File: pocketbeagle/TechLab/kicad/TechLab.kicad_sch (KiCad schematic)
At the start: 82 parts, among them T1 3904, T2 EAALSTIC1708A0, U1 CAT24C32, U2 TPD4S012DRY, U3 MMA8453Q, U4 TPS2051CDBV, U5 MCP23S18-E/MJ, U6 FT230XQ-R, X1 292303-1, X2 10118192-0001LF

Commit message: Convert Techlab to multisheet schematic
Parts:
- removed BUZZER0: SMD-140035H, TechLab:SMD-140035H, symbol TechLab-eagle-import:SMD-140035H
- removed C1, C10, C2, C3, C4, C5, C8, C9: .1uF, TechLab:0402, symbol TechLab-eagle-import:CAPACITOR-(INCH)-0402
- removed C11: 10nF, TechLab:0402, symbol TechLab-eagle-import:CAPACITOR-(INCH)-0402
- removed C6: 4.7uF, TechLab:0402, symbol TechLab-eagle-import:CAPACITOR-(INCH)-0402
- removed C7: 10uF, 6.3V, TechLab:0805, symbol TechLab-eagle-import:CAPACITOR-(INCH)-0805
- removed EXP1: PARALLEL-8PIN-0.9INCH_PITCH-SMT_GP, TechLab:PARALLEL-8PIN-0.9INCH_PITCH-SMT_GP, symbol TechLab-eagle-import:PARALLEL-8PIN-0.9INCH_PITCH-SMT_GP
- removed F1, F2: 1206L025YR, TechLab:1206, symbol TechLab-eagle-import:FUSE-(INCH)-1206
- removed FB1, FB2, FB3, FB4: 120 Ohm (BLM18AG121SN1D), TechLab:0603, symbol TechLab-eagle-import:FB-(INCH)-0603
- removed FUD1, FUD2, FUD3: FIDUCIAL, TechLab:FIDUCIAL_40MIL, symbol TechLab-eagle-import:FIDUCIAL
- removed JMP1: JUMPER-(X2), TechLab:JUMPER-(X2), symbol TechLab-eagle-import:JUMPER-(X2)
- removed L.BTN0, R.BTN0: TACTILE.SWITCH-6MM, TechLab:6MM_TACTILE-SWITCH, symbol TechLab-eagle-import:TACTILE.SWITCH-6MM
- removed LD1: JNS-5050RGB, TechLab:LED_RGB_5050, symbol TechLab-eagle-import:JNS-5050RGB
- removed LD10, LD11, LD12, LD13, LD14, LD15, LD2, LD3, LD4, LD5, LD6, LD7, LD8, LD9, TX0: GREEN, TechLab:0805-LED, symbol TechLab-eagle-import:LED-(INCH)-0805
- removed POCKETBEAGLE-1: POCKETBEAGLE-(ORIGIN-CENTER)-SMT.PADS(ONLY)-NO.RE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, TechLab:POCKETBEAGLE-(ORIGIN-CENTER)-SMT.PADS(ONLY)-NO.RESTRICT, symbol TechLab-eagle-import:POCKETBEAGLE-(ORIGIN-CENTER)-SMT.PADS(ONLY)-NO.RESTRICT
- removed R1, R2: 1.5k, TechLab:0402, symbol TechLab-eagle-import:RESISTOR-(INCH)-0402
- removed R10, R19, R20, R9: 33, TechLab:0402, symbol TechLab-eagle-import:RESISTOR-(INCH)-0402
- removed R11, R12, R13, R14, R21, R22, R3, R4: 1k, TechLab:0402, symbol TechLab-eagle-import:RESISTOR-(INCH)-0402
- removed R15, R16: DNP(2.2k), TechLab:0402, symbol TechLab-eagle-import:RESISTOR-(INCH)-0402
- removed R17, R18, R5: 4.7k, TechLab:0402, symbol TechLab-eagle-import:RESISTOR-(INCH)-0402
- removed R6: 100k, TechLab:0402, symbol TechLab-eagle-import:RESISTOR-(INCH)-0402
- removed R7: DNP(1.5k), TechLab:0402, symbol TechLab-eagle-import:RESISTOR-(INCH)-0402
- removed R8: 0, TechLab:0402, symbol TechLab-eagle-import:RESISTOR-(INCH)-0402
- removed RESET.BTN0: TACTILE.SWITCH-3X3.5MM, TechLab:3X3.5MM-TACTILE-SWITCH, symbol TechLab-eagle-import:TACTILE.SWITCH-3X3.5MM
- removed RN1, RN2, RN3, RN4: 1k, TechLab:RN0804, symbol TechLab-eagle-import:RESISTOR.NETWORK-(4)
- removed RX0: RED, TechLab:0805-LED, symbol TechLab-eagle-import:LED-(INCH)-0805
- removed SJ1, SJ2: SOLDER.JOINT-(INCH)-0402, TechLab:SOLDER.JOINT(0402), symbol TechLab-eagle-import:SOLDER.JOINT-(INCH)-0402
- removed T1: 3904, TechLab:SOT23, symbol TechLab-eagle-import:NPN.BIPOLAR-(SOT23)
- removed T2: EAALSTIC1708A0, TechLab:EAALSTIC1708A0, symbol TechLab-eagle-import:EAALSTIC1708A0
- removed U1: CAT24C32, TechLab:UDFN8,2X3(ON-SEMI), symbol TechLab-eagle-import:CAT24C32
- removed U2: TPD4S012DRY, TechLab:SON-6(TI)-DRY, symbol TechLab-eagle-import:TPD4S012DRYR
- removed U3: MMA8453Q, TechLab:QFN-16-(MMA8453Q), symbol TechLab-eagle-import:MMA8453Q
- removed U4: TPS2051CDBV, TechLab:SOT23-5(TI-DBV), symbol TechLab-eagle-import:TPS2051CDBV
- removed U5: MCP23S18-E/MJ, TechLab:QFN24-MJ-0.5-4X4MM, symbol TechLab-eagle-import:MCP23S18
- removed U6: FT230XQ-R, TechLab:QFN16-0.65-4X4MM, symbol TechLab-eagle-import:FT230XQ
- removed X1: 292303-1, TechLab:292303-1, symbol TechLab-eagle-import:292303-1
- removed X2: 10118192-0001LF, TechLab:10118192-0001LF(MICRO-USB-B-AMPHENOL-FCI), symbol TechLab-eagle-import:10118192-0001LF
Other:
- added sheet Page1 (TechLab_page1.kicad_sch)
- added sheet Page2 (TechLab_Page2.kicad_sch)
- note removed: "------------------------------"
- note removed: "0 | 1 | 0 | 1 | A2 | A1 | A0 | R/W"
- note removed: "1 | 0 | 1 | 0 | H | H | H | R/W = 0x57"
- note removed: "1 | 0 | 1 | 0 | H | H | L | R/W = 0x56"
- note removed: "1 | 0 | 1 | 0 | H | L | H | R/W = 0x55"
- note removed: "1 | 0 | 1 | 0 | H | L | L | R/W = 0x54"
- note removed: "1 | 0 | 1 | 0 | L | H | H | R/W = 0x53"
- note removed: "1 | 0 | 1 | 0 | L | H | L | R/W = 0x52"
- note removed: "1 | 0 | 1 | 0 | L | L | H | R/W = 0x51"
- note removed: "1 | 0 | 1 | 0 | L | L | L | R/W = 0x50"
- note removed: "Accelerometer"
- note removed: "Buttons"
- note removed: "Buzzer"
- note removed: "Datasheet indicates all pins 1, 2, and 3 have the exact same ESD protection and are interchangeable."
- note removed: "Light Sensor"
- note removed: "Multi-colored LED (Bulb)"
- note removed: "Slave Address SA0~ High: 0011101 (0x1D) Low: 0011100 (0x1C)"

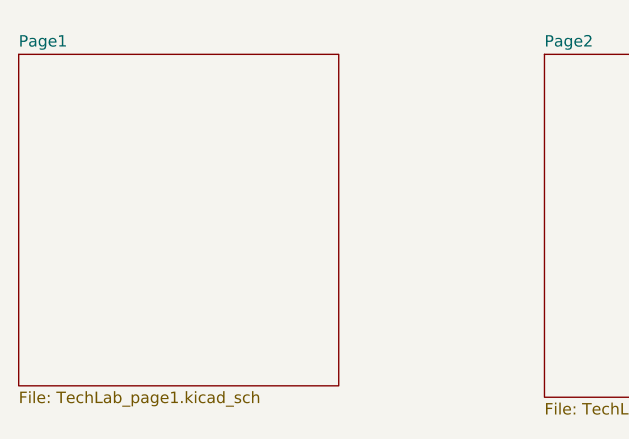
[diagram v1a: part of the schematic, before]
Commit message: TechLab: Update title block for cleaner print
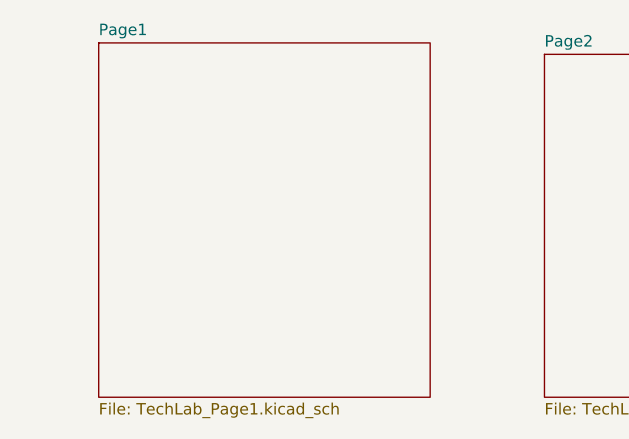
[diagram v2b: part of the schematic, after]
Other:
- sheet Page1: file TechLab_page1.kicad_sch -> TechLab_Page1.kicad_sch
- company: (none) -> BeagleBoard.org Foundation
- title: (none) -> PocketBeagle TechLab
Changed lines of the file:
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@@
 	(generator "eeschema")
 	(generator_version "8.0")
-	(paper "User" 601.98 254.127)
+	(paper "A")
+	(title_block
+		(title "PocketBeagle TechLab")
+		(date "2025-04-23")
+		(rev "A5")
+		(company "BeagleBoard.org Foundation")
+	)
+	(sheet
+		(at 35.56 29.21)
+		(size 36.83 39.37)
+		(fields_autoplaced yes)
+		(stroke
+			(width 0.1524)
+			(type solid)
+		)
+		(fill
+			(color 0 0 0 0.0000)
+		)
+		(property "Sheetname" "Page1"
+			(at 35.56 28.4984 0)
+			(effects
+				(font
+					(size 1.27 1.27)
+				)
+				(justify left bottom)
+			)
+		)
+		(property "Sheetfile" "TechLab_Page1.kicad_sch"
+			(at 35.56 69.1646 0)
+			(effects
+				(font
+					(size 1.27 1.27)
+				)
+				(justify left top)
+			)
+		)
+		(instances
+			(project "TechLab"
+				(path "/199e843b-8c9a-4ca8-a6e6-fde18a374d00"
+					(page "1")
+				)
+			)
+		)
+	)
 	(sheet
 		(at 85.09 30.48)
@@
 				)
 			)
-		)
-	)
-	(sheet
-		(at 26.67 30.48)
-		(size 35.56 36.83)
-		(fields_autoplaced yes)
-		(stroke
-			(width 0.1524)
-			(type solid)
-		)
-		(fill
-			(color 0 0 0 0.0000)
-		)
-		(property "Sheetname" "Page1"
-			(at 26.67 29.7684 0)
-			(effects
-				(font
-					(size 1.27 1.27)
-				)
-				(justify left bottom)
-			)
-		)
-		(property "Sheetfile" "TechLab_page1.kicad_sch"
-			(at 26.67 67.8946 0)
-			(effects
-				(font
-					(size 1.27 1.27)
-				)
-				(justify left top)
-			)
-		)
-		(instances
-			(project "TechLab"
-				(path "/199e843b-8c9a-4ca8-a6e6-fde18a374d00"
-					(page "1")
-				)
-			)
